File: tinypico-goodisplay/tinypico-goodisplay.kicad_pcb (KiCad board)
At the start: 2 copper layers, 21 parts, among them Q1 Si1308, U1 TinypicoESP32_Symbol, U2 FPCConn

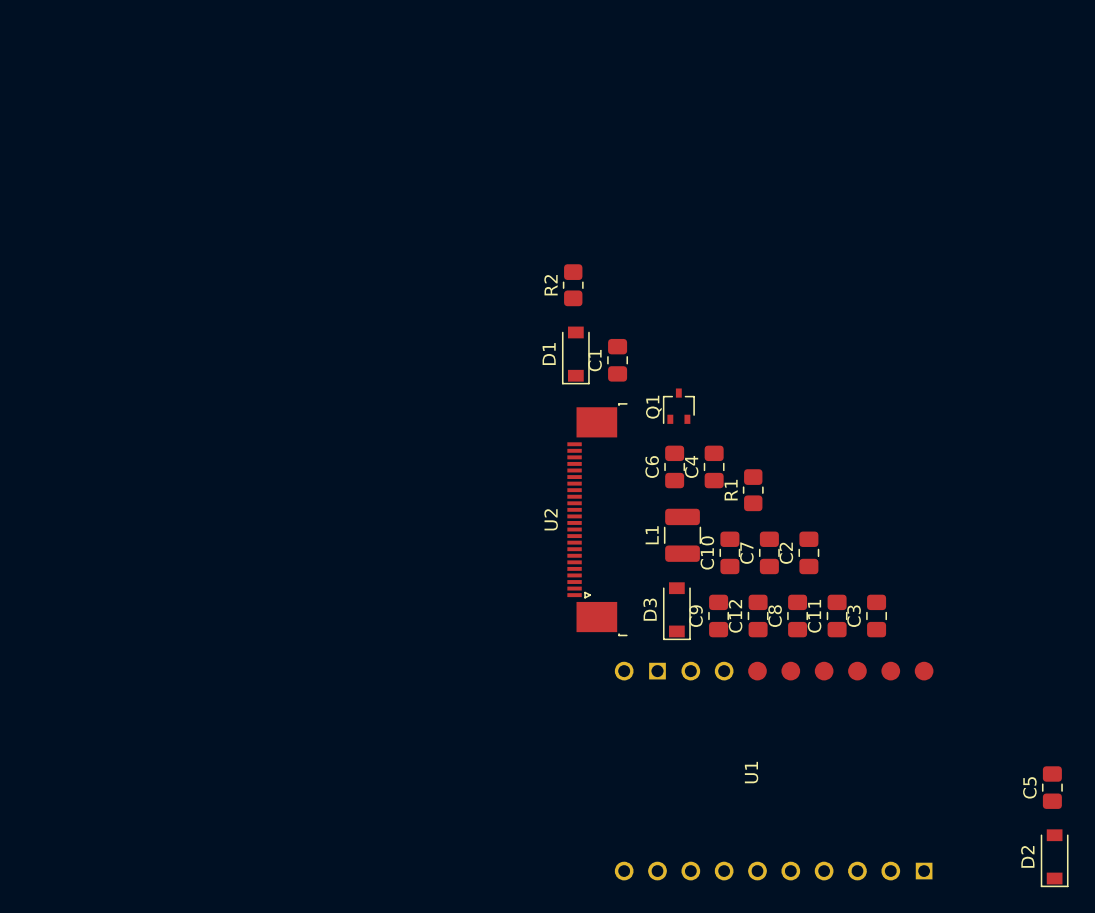
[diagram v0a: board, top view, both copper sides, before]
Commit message: PCB passes DRC
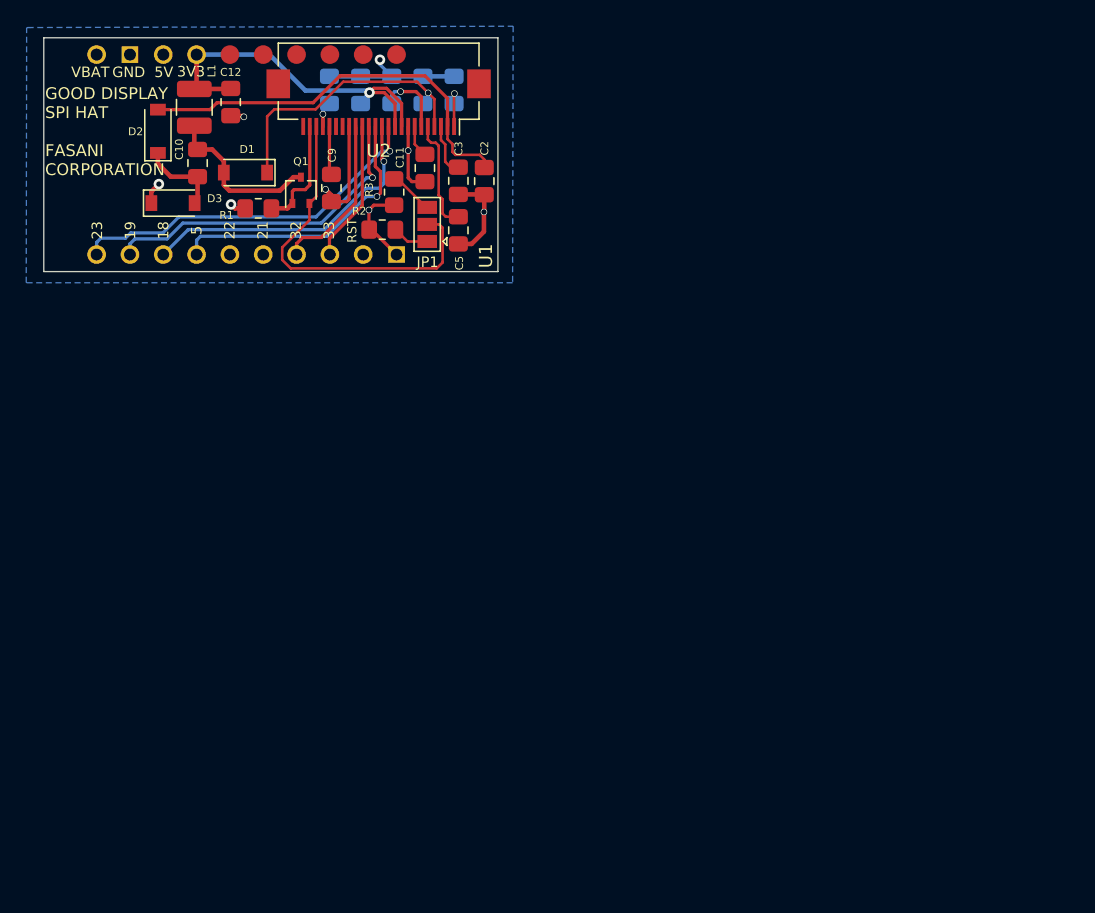
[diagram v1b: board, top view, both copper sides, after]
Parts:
- added JP1: selector, Jumper:SolderJumper-3_P1.3mm_Open_Pad1.0x1.5mm, F.Cu at (101.5, 49.0)
- added R3: 3R, Resistor_SMD:R_0805_2012Metric_Pad1.20x1.40mm_HandSolder, F.Cu at (98.9, 46.6)
- C1, C4, C6, C7, C8: moved to B.Cu
- U2: footprint Connector_FFC-FPC:TE_2-1734839-4_1x24-1MP_P0.5mm_Horizontal -> footprint:Hirose_FH12-24S-0.5SH_1x24-1MP_P0.50mm_Horizontal
- moved D2 87.9 mm to (80.9, 41.9)
- moved C5 62.1 mm to (103.8, 49.5)
- moved U1 61.8 mm to (90.2, 43.8)
- moved C12 56.1 mm to (86.5, 39.7)
- moved C8 52.1 mm to (96.4, 38.8), turned to -90 degrees
- moved C10 50.3 mm to (84.0, 44.4), turned to -90 degrees
- moved L1 49.5 mm to (83.7, 40.1)
- moved D3 49.4 mm to (82.1, 47.4), turned to 0 degrees
- moved C7 48.7 mm to (94.0, 38.8), turned to -90 degrees
- moved C11 46.4 mm to (101.3, 44.7)
- moved C3 46.0 mm to (103.8, 45.7)
- moved C9 44.0 mm to (94.2, 46.2)
- moved R1 43.4 mm to (88.6, 47.8), turned to 180 degrees
- moved C2 37.6 mm to (105.8, 45.7)
- moved C4 36.3 mm to (101.1, 38.8), turned to -90 degrees
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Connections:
- C8 pad 2: +3.3VP -> +3V3
- Q1 pad 2: Net-(Q1-Pad2) -> Net-(JP1-Pad2)
- R2 pad 1: Net-(Q1-Pad2) -> Net-(JP1-Pad1)
- U2 pad 10: +3.3VP -> +3V3
- U2 pad 22: Net-(Q1-Pad2) -> Net-(JP1-Pad2)
- U2 pad 9: +3.3VP -> +3V3
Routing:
- net GND: track 0.00 -> 42.6 mm, vias 0 -> 8
- net Net-(C2-Pad2): track 0.00 -> 31.3 mm
- net +3V3: track 0.00 -> 29.7 mm, vias 0 -> 1
- net /EPD_MOSI: track 0.00 -> 28.1 mm, vias 0 -> 1
- net Net-(JP1-Pad2): track 0.00 -> 27.9 mm
- net /EPD_DC: track 0.00 -> 25.4 mm, vias 0 -> 1
- net /EPD_CLK: track 0.00 -> 23.5 mm, vias 0 -> 1
- net /EPD_CS: track 0.00 -> 21.8 mm, vias 0 -> 1
- net Net-(C4-Pad2): track 0.00 -> 21.7 mm, vias 0 -> 1
- net Net-(C10-Pad1): track 0.00 -> 12.6 mm
- net /EPD_BUSY: track 0.00 -> 12.5 mm
- net /EPD_RST: track 0.00 -> 10.8 mm
- net Net-(Q1-Pad1): track 0.00 -> 8.67 mm
- net Net-(C5-Pad2): track 0.00 -> 8.61 mm
- net Net-(C10-Pad2): track 0.00 -> 6.36 mm
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- added copper zone on B.Cu, net GND
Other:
- board outline added: 34.6 x 17.8 mm
- board text added: "18"
- board text added: "19"
- board text added: "21"
- board text added: "22"
- board text added: "23"
- board text added: "32"
- board text added: "33"
- board text added: "3V3"
- board text added: "5"
- board text added: "5V"
- board text added: "GND"
- board text added: "GOOD DISPLAY SPI HAT FASANI CORPORATION"
- board text added: "RST"
- board text added: "VBAT"

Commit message: Update Silk
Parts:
- moved JP1 0.43 mm to (101.4, 49.5)
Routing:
- net Net-(JP1-Pad2): track 27.9 -> 27.3 mm
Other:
- board text added: "0.47"
- board text added: "3"
- board text added: "FASANI CORPORATION"
- board text added: "GOODISPLAY SPI HAT"
- board text removed: "GOOD DISPLAY SPI HAT FASANI CORPORATION"
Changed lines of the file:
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@@
     (property "Sheetname" "")
     (attr smd)
-    (fp_text reference "C12" (at 2.275 0 180) (layer "F.SilkS")
+    (fp_text reference "C12" (at 0.15 1.475 270) (layer "F.SilkS")
       (effects (font (size 0.6 0.6) (thickness 0.12)))
     )
@@
     (property "Sheetname" "")
     (attr smd)
-    (fp_text reference "U2" (at 0 -3.7) (layer "F.SilkS")
+    (fp_text reference "U2" (at 0 -3.7) (layer "F.SilkS") hide
       (effects (font (size 1 1) (thickness 0.15)))
     )
@@
   )
   (footprint "Jumper:SolderJumper-3_P1.3mm_Open_Pad1.0x1.5mm" (layer "F.Cu")
-    (at 101.45 49.025 90)
+    (at 101.4 49.45 90)
     (descr "SMD Solder 3-pad Jumper, 1x1.5mm Pads, 0.3mm gap, open")
     (tags "solder jumper open")
@@
     (property "Sheetname" "")
     (attr exclude_from_pos_files)
-    (fp_text reference "JP1" (at -2.875 0.025 180) (layer "F.SilkS")
-      (effects (font (size 0.8 0.8) (thickness 0.12)))
+    (fp_text reference "JP1" (at -2.75 -0.675 180) (layer "F.SilkS") hide
+      (effects (font (size 0.6 0.6) (thickness 0.12)))
     )
     (fp_text value "selector" (at 0 2 90) (layer "F.Fab")
@@
     (property "Sheetname" "")
     (attr smd)
-    (fp_text reference "L1" (at 2.775 1.325 90) (layer "F.SilkS")
+    (fp_text reference "L1" (at -2 1.95 90) (layer "F.SilkS")
       (effects (font (size 0.6 0.6) (thickness 0.12)))
     )
@@
     (property "Sheetname" "")
     (attr through_hole)
-    (fp_text reference "U1" (at -7.615 15.735 90 unlocked) (layer "F.SilkS")
+    (fp_text reference "U1" (at -7.615 15.735 90 unlocked) (layer "F.SilkS") hide
       (effects (font (size 1 1) (thickness 0.15)))
     )
@@
   (gr_line (start 106.84 34.8) (end 72.23 34.8) (layer "Edge.Cuts") (width 0.1))
   (gr_line (start 106.84 52.62) (end 106.84 34.8) (layer "Edge.Cuts") (width 0.1))
-  (gr_text "3V3" (at 83.45 37.375) (layer "F.SilkS")
-    (effects (font (size 0.8 0.8) (thickness 0.12)))
+  (gr_text "FASANI\nCORPORATION" (at 74.125 50.35 90) (layer "F.Cu")
+    (effects (font (size 0.8 0.8) (thickness 0.13)) (justify left))
+  )
+  (gr_text "3V3" (at 83.85 37.4) (layer "F.SilkS")
+    (effects (font (size 0.7 0.7) (thickness 0.12)))
   )
   (gr_text "32" (at 91.45 49.475 90) (layer "F.SilkS")
@@
     (effects (font (size 0.8 0.8) (thickness 0.12)))
   )
-  (gr_text "5V" (at 81.375 37.425) (layer "F.SilkS")
+  (gr_text "5V" (at 81.3 37.7) (layer "F.SilkS")
     (effects (font (size 0.8 0.8) (thickness 0.12)))
   )
-  (gr_text "GND" (at 78.7 37.425) (layer "F.SilkS")
+  (gr_text "3" (at 101.5 46.875 90) (layer "F.SilkS")
+    (effects (font (size 0.6 0.6) (thickness 0.12)))
+  )
+  (gr_text "0.47" (at 101.425 52.2) (layer "F.SilkS")
+    (effects (font (size 0.6 0.6) (thickness 0.12)))
+  )
+  (gr_text "GND" (at 78.75 37.7) (layer "F.SilkS")
     (effects (font (size 0.8 0.8) (thickness 0.12)))
   )
@@
     (effects (font (size 0.7 0.7) (thickness 0.12)))
   )
-  (gr_text "GOOD DISPLAY\nSPI HAT\n\nFASANI\nCORPORATION" (at 72.325 41.95) (layer "F.SilkS")
-    (effects (font (size 0.9 0.9) (thickness 0.13)) (justify left))
-  )
-  (gr_text "VBAT" (at 75.775 37.425) (layer "F.SilkS")
+  (gr_text "GOODISPLAY\nSPI HAT" (at 72.725 39.85) (layer "F.SilkS")
+    (effects (font (size 1 1) (thickness 0.13)) (justify left))
+  )
+  (gr_text "VBAT" (at 75.825 37.7) (layer "F.SilkS")
     (effects (font (size 0.8 0.8) (thickness 0.12)))
   )
@@
   (segment (start 100.5 41.56) (end 100.5 42.9125) (width 0.2) (layer "F.Cu") (net 30))
   (segment (start 100.5 42.9125) (end 101.275 43.6875) (width 0.2) (layer "F.Cu") (net 30))
-  (segment (start 99.21 45.56) (end 101.375 47.725) (width 0.2) (layer "F.Cu") (net 31))
-  (segment (start 98.93 45.56) (end 99.21 45.56) (width 0.2) (layer "F.Cu") (net 31))
-  (segment (start 101.375 47.725) (end 101.45 47.725) (width 0.2) (layer "F.Cu") (net 31))
+  (segment (start 98.93 45.68) (end 101.4 48.15) (width 0.35) (layer "F.Cu") (net 31))
+  (segment (start 98.93 45.56) (end 98.93 45.68) (width 0.35) (layer "F.Cu") (net 31))
   (segment (start 91.05 52.375) (end 102.175 52.375) (width 0.2) (layer "F.Cu") (net 32))
   (segment (start 90.4 51.725) (end 91.05 52.375) (width 0.2) (layer "F.Cu") (net 32))
@@
   (segment (start 92.475 47.425) (end 92.475 48.7) (width 0.2) (layer "F.Cu") (net 32))
   (segment (start 90.4 50.775) (end 90.4 51.725) (width 0.2) (layer "F.Cu") (net 32))
-  (segment (start 102.375 49.025) (end 101.45 49.025) (width 0.2) (layer "F.Cu") (net 32))
-  (segment (start 102.625 51.925) (end 102.625 49.275) (width 0.2) (layer "F.Cu") (net 32))
+  (segment (start 102.625 49.925) (end 102.15 49.45) (width 0.2) (layer "F.Cu") (net 32))
+  (segment (start 102.15 49.45) (end 101.4 49.45) (width 0.2) (layer "F.Cu") (net 32))
   (segment (start 93 46.9) (end 92.475 47.425) (width 0.2) (layer "F.Cu") (net 32))
   (segment (start 102.175 52.375) (end 102.625 51.925) (width 0.2) (layer "F.Cu") (net 32))
   (segment (start 93 41.56) (end 93 46.9) (width 0.2) (layer "F.Cu") (net 32))
-  (segment (start 102.625 49.275) (end 102.375 49.025) (width 0.2) (layer "F.Cu") (net 32))
-  (segment (start 99.95 50.325) (end 101.45 50.325) (width 0.2) (layer "F.Cu") (net 33))
-  (segment (start 99.01 49.385) (end 99.95 50.325) (width 0.2) (layer "F.Cu") (net 33))
+  (segment (start 102.625 51.925) (end 102.625 49.925) (width 0.2) (layer "F.Cu") (net 32))
+  (segment (start 99.325 49.425) (end 100.65 50.75) (width 0.35) (layer "F.Cu") (net 33))
+  (segment (start 100.65 50.75) (end 101.4 50.75) (width 0.35) (layer "F.Cu") (net 33))
+  (segment (start 99.025 49.425) (end 99.325 49.425) (width 0.35) (layer "F.Cu") (net 33))
   (segment (start 91.175 46.5) (end 91.175 47.425) (width 0.25) (layer "F.Cu") (net 34))
   (segment (start 92.15 46.375) (end 91.3 46.375) (width 0.25) (layer "F.Cu") (net 34))

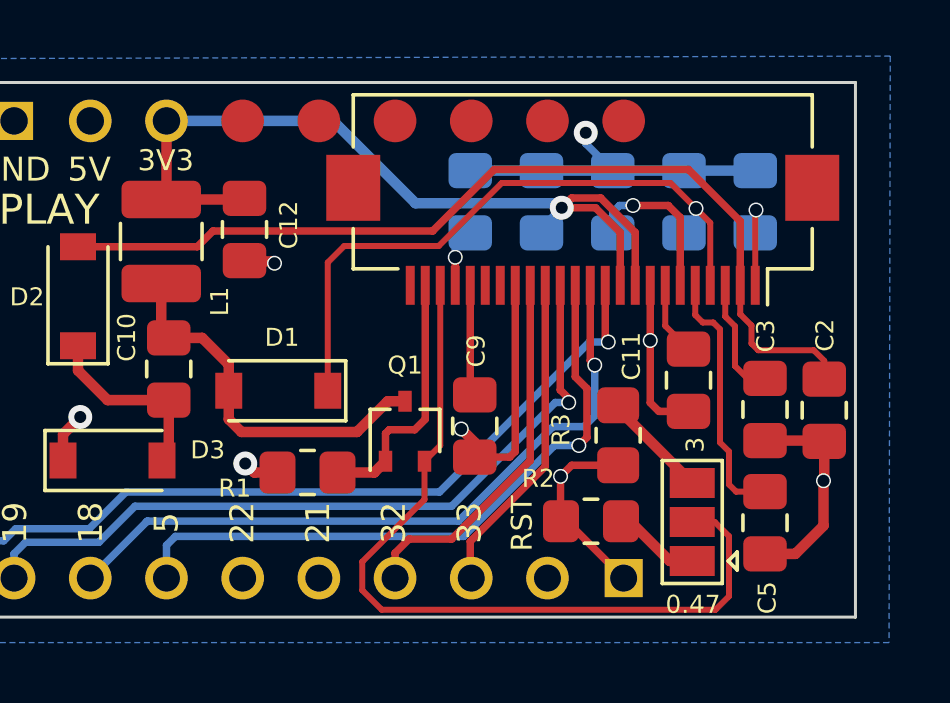
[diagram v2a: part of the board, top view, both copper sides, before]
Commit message: Min. VIA when PCB is 2 layer is 0.6mm
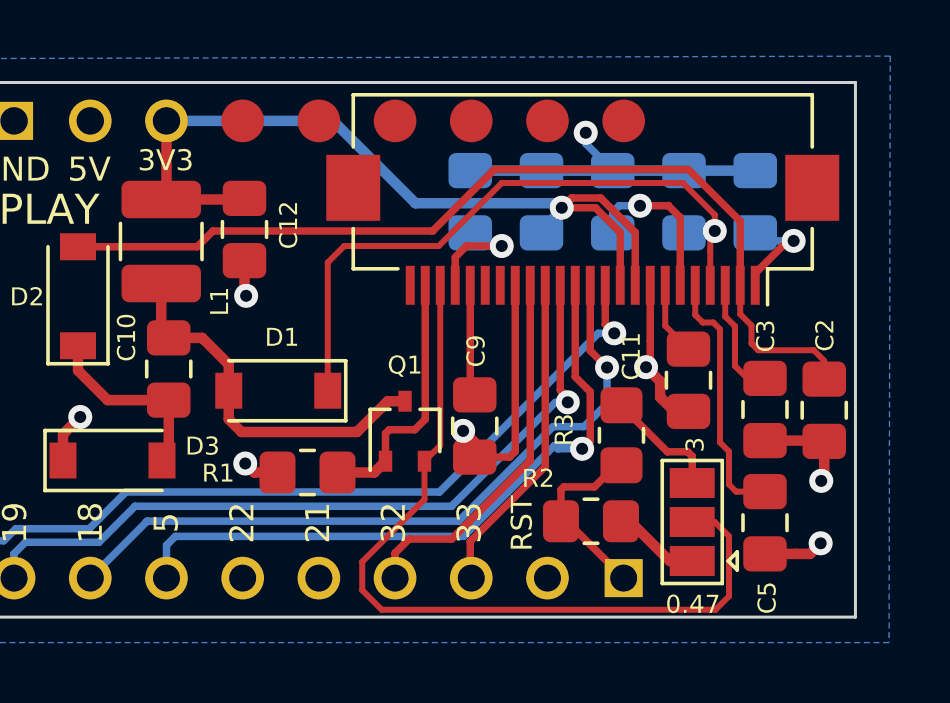
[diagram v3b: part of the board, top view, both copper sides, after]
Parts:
- moved R3 0.11 mm to (99.0, 46.6)
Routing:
- net Net-(C7-Pad2): track 1.70 -> 3.87 mm
- net GND: track 42.6 -> 40.8 mm
- net /EPD_CS: track 21.8 -> 23.0 mm
- net Net-(C4-Pad2): track 21.7 -> 22.4 mm

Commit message: Update Silk
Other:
- board text added: "1"
- board text added: "24"
- board text added: "V1.0"
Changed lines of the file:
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@@
     (property "Sheetname" "")
     (attr smd)
-    (fp_text reference "R1" (at 2.975 -0.025) (layer "F.SilkS")
+    (fp_text reference "R1" (at 2.405 1.12) (layer "F.SilkS")
       (effects (font (size 0.6 0.6) (thickness 0.12)))
     )
@@
     (property "Sheetname" "")
     (attr smd)
-    (fp_text reference "D3" (at 3 -0.475) (layer "F.SilkS")
+    (fp_text reference "D3" (at 2.955 -0.1) (layer "F.SilkS")
       (effects (font (size 0.6 0.6) (thickness 0.12)))
     )
@@
     (property "Sheetname" "")
     (attr smd)
-    (fp_text reference "R2" (at 1.76 1.425) (layer "F.SilkS")
+    (fp_text reference "R2" (at 1.355 1.605) (layer "F.SilkS")
       (effects (font (size 0.6 0.6) (thickness 0.12)))
     )
@@
     (effects (font (size 0.7 0.7) (thickness 0.12)))
   )
+  (gr_text "24" (at 90.64 41.86) (layer "F.SilkS")
+    (effects (font (size 1 1) (thickness 0.15)))
+  )
   (gr_text "32" (at 91.45 49.475 90) (layer "F.SilkS")
     (effects (font (size 0.8 0.8) (thickness 0.12)))
@@
     (effects (font (size 0.8 0.8) (thickness 0.12)))
   )
+  (gr_text "V1.0" (at 77.78 45.17) (layer "F.SilkS")
+    (effects (font (size 0.8 0.8) (thickness 0.12)))
+  )
+  (gr_text "1" (at 104.57 41.86) (layer "F.SilkS")
+    (effects (font (size 1 1) (thickness 0.15)))
+  )
   (gr_text "3" (at 101.5 46.875 90) (layer "F.SilkS")

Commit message: Update C4
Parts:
- C8: moved to F.Cu
- moved C8 8.78 mm to (87.7, 39.8), turned to 90 degrees
- moved C12 0.97 mm to (85.5, 39.8)
- moved D2 0.90 mm to (80.0, 42.0)
- moved L1 0.90 mm to (82.8, 40.2)
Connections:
- C1 pad 2: Net-(C1-Pad2) -> /VCOM
- U1 pad 5: unconnected-(U1-Pad5) -> /VCOM
- U2 pad 1: Net-(C1-Pad2) -> /VCOM
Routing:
- net /VCOM: track 0.00 -> 25.6 mm, vias 0 -> 1
- net +3V3: track 29.7 -> 35.0 mm
- net GND: track 40.8 -> 44.8 mm
- net Net-(C1-Pad2): track 3.52 -> 0.00 mm, vias 1 -> 0
- net Net-(C2-Pad2): track 31.3 -> 32.5 mm
- net Net-(C10-Pad2): track 6.36 -> 7.18 mm
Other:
- board text added: "VCOM"

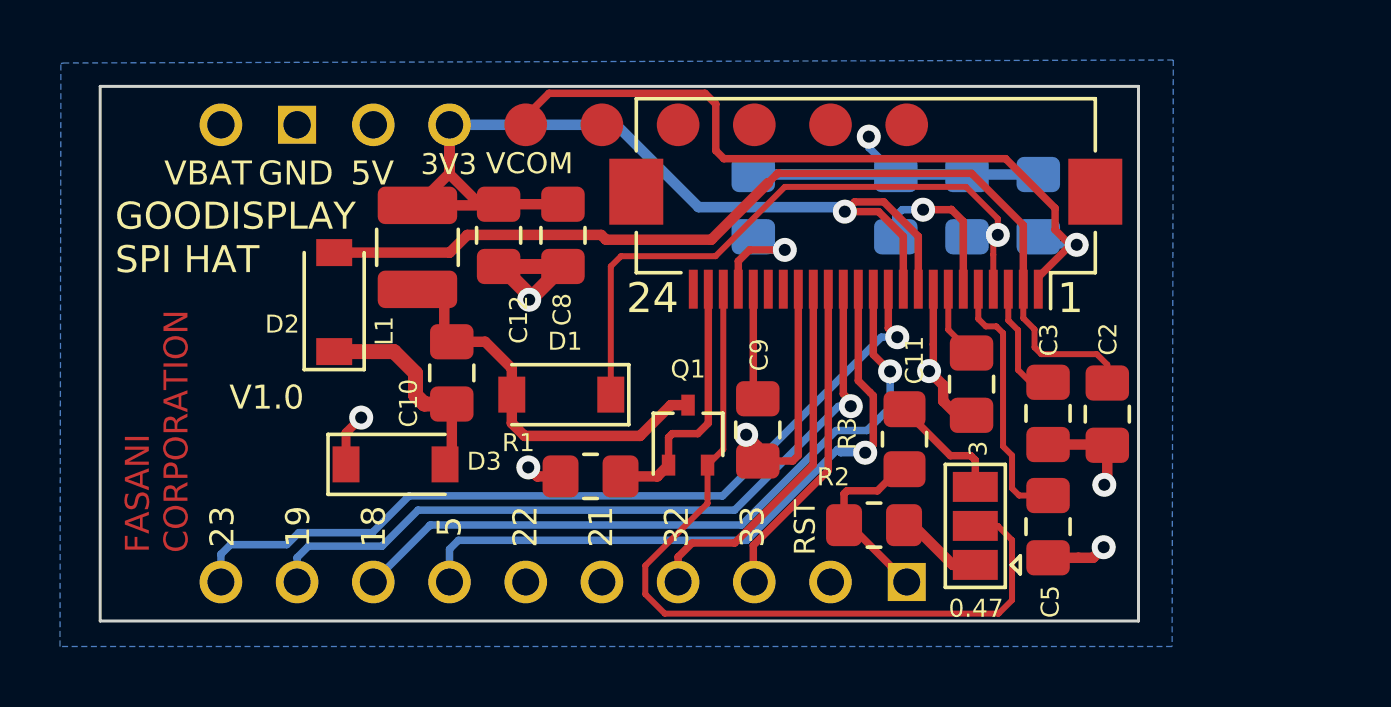
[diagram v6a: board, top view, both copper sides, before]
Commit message: Add RES switch
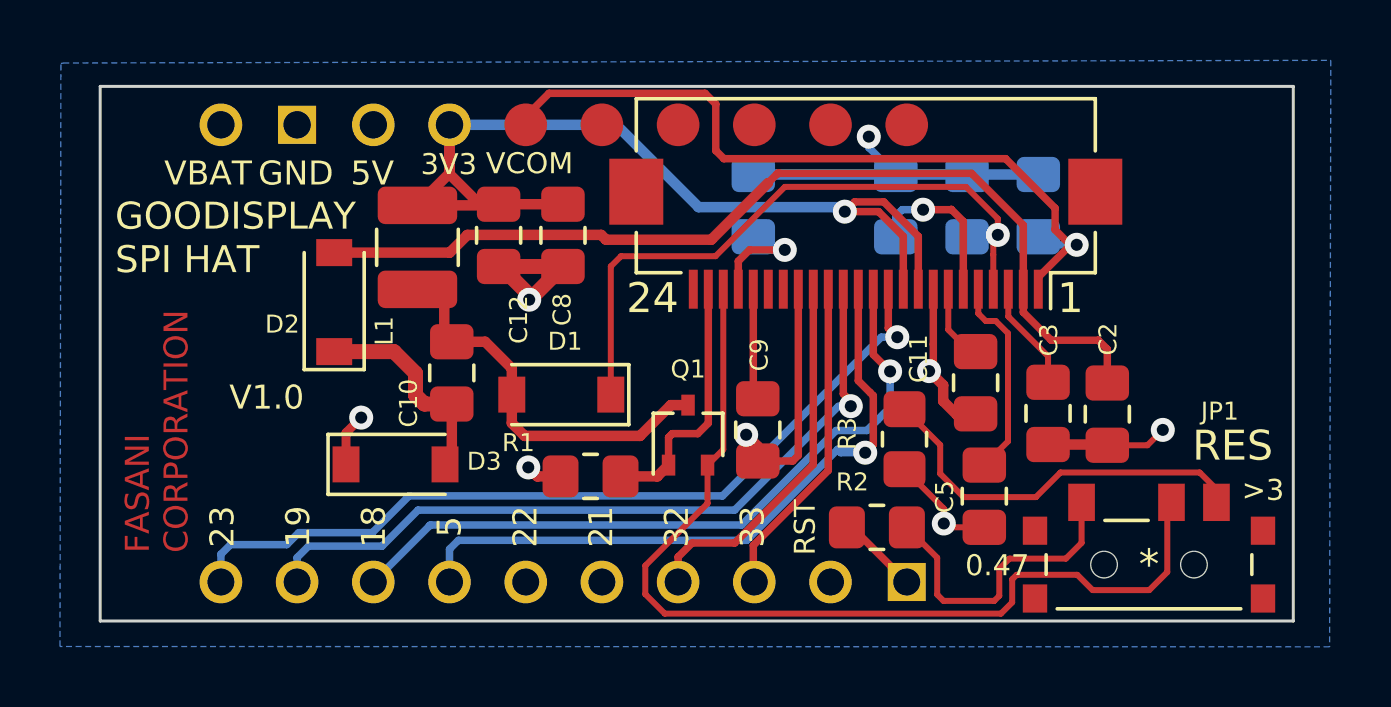
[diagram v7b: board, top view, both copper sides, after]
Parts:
- JP1: footprint Jumper:SolderJumper-3_P1.3mm_Open_Pad1.0x1.5mm -> footprint:switch-MK-12C02-G020
- moved JP1 5.93 mm to (107.2, 50.7), turned to 0 degrees
- moved C5 2.35 mm to (101.7, 48.5)
- moved C11 0.14 mm to (101.4, 44.7)
- moved R2 0.12 mm to (98.1, 49.5)
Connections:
- U2 pad P1: (no net) -> unconnected-(U2-PadP1)
- U2 pad P2: (no net) -> unconnected-(U2-PadP2)
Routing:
- net Net-(JP1-Pad3): track 3.97 -> 13.2 mm
- net Net-(JP1-Pad1): track 2.92 -> 10.2 mm
- net Net-(JP1-Pad2): track 27.3 -> 32.7 mm
- net Net-(C5-Pad2): track 8.61 -> 6.79 mm
- net GND: track 44.8 -> 43.7 mm
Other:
- board size 34.6 x 17.8 mm -> 39.8 x 17.8 mm
- board text added: ">3"
- board text added: "RES"
- board text removed: "3"
